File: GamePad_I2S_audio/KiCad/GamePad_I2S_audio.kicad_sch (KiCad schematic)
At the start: 75 parts, among them IC1 PCM5100, IC2 PAM8908, J1 Conn_02x17_Odd_Even

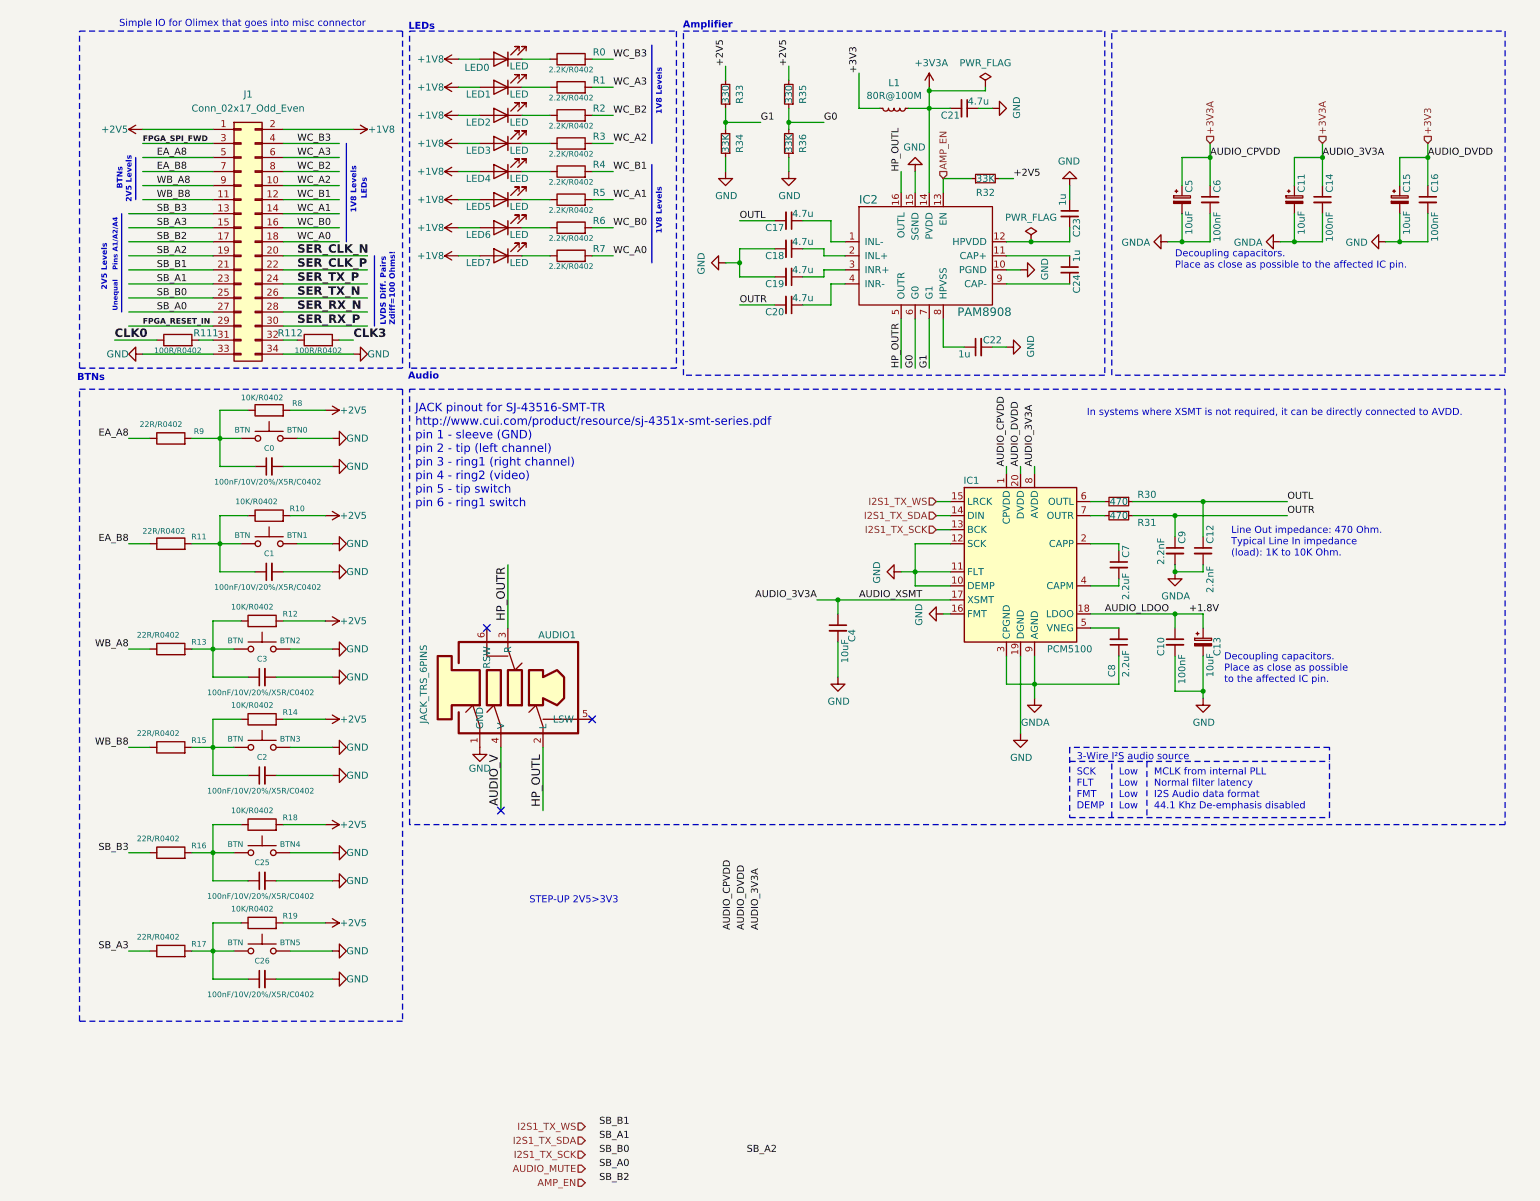
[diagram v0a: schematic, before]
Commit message: Adding StepUP
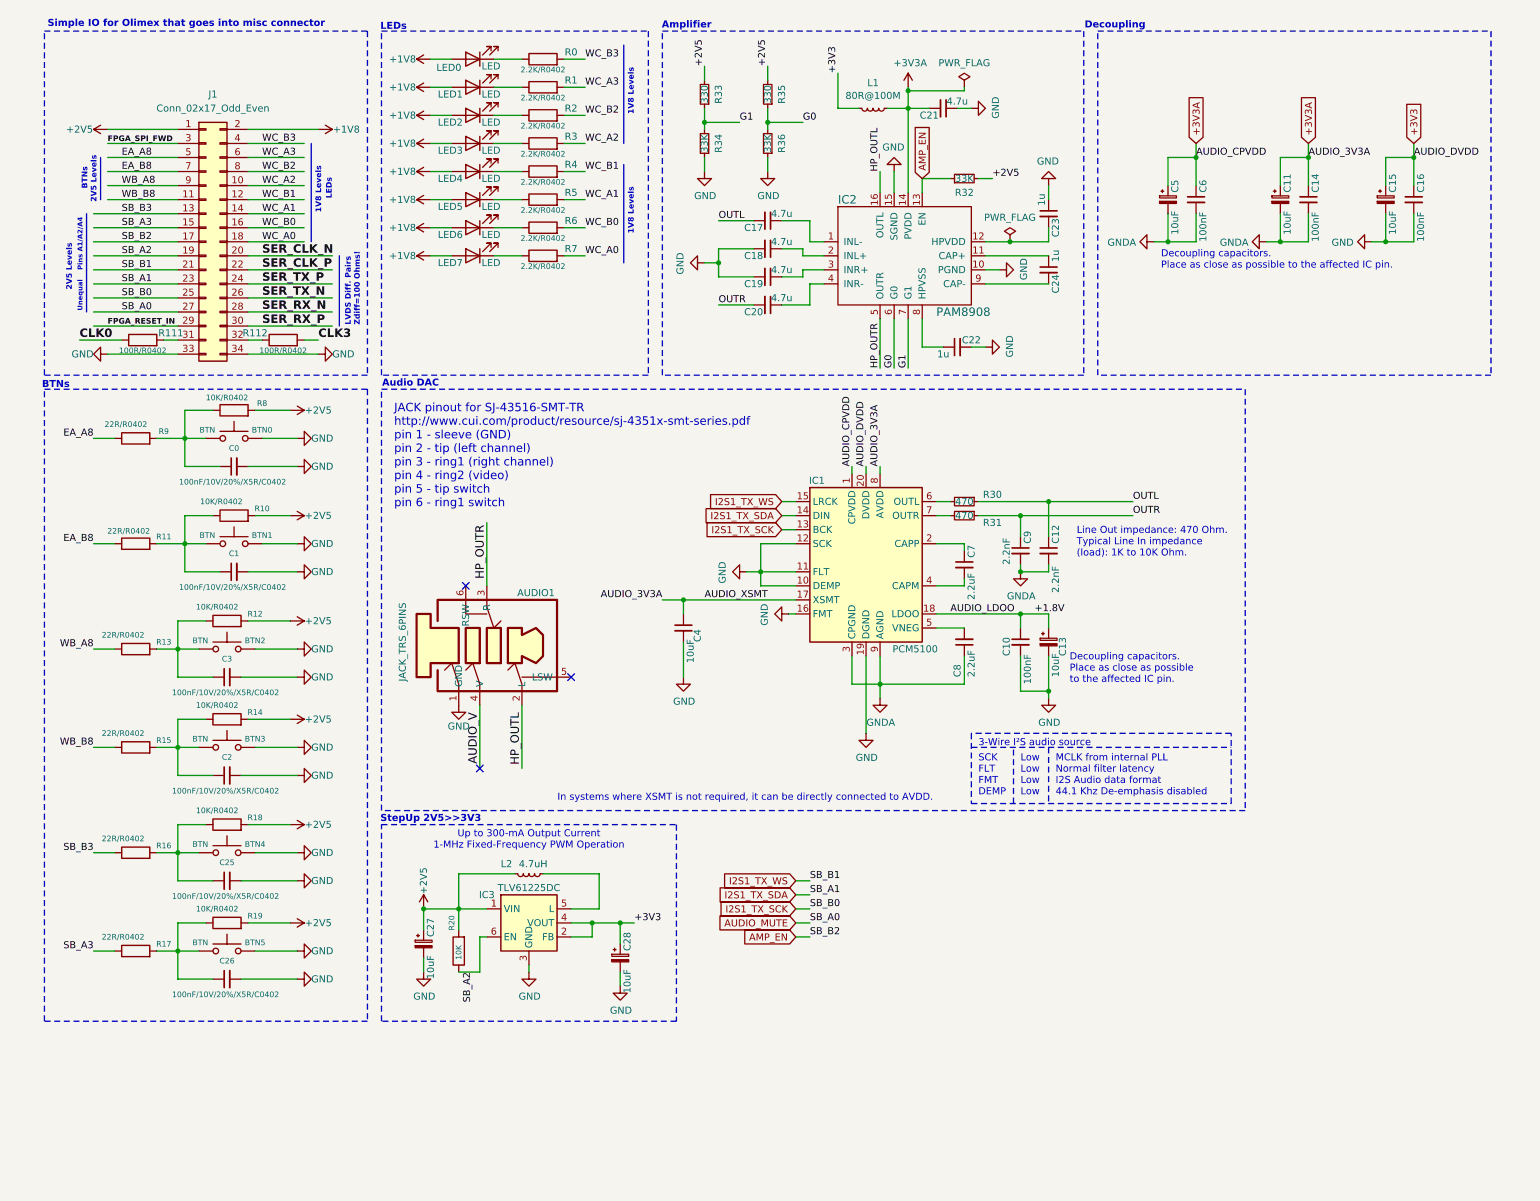
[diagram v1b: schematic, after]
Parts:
- added C27, C28: 10uF, Capacitor_SMD:C_1206_3216Metric, symbol Device:CP_Small
- added IC3: TLV61225DC, Package_TO_SOT_SMD:SOT-363_SC-70-6, symbol Regulator_Switching:TLV61225DC
- added L2: 4.7uH, Inductor_SMD:L_0603_1608Metric, symbol Device:L_Small
- added R20: 10K, Resistor_SMD:R_0603_1608Metric, symbol OLIMEX_RCL:R
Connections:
- net SB_A0 is gone; now on net AUDIO_MUTE: J1.27 (Pin_27)
- net SB_A1 is gone; now on net I2S1_TX_SDA: J1.23 (Pin_23)
- net SB_B0 is gone; now on net I2S1_TX_SCK: J1.25 (Pin_25)
- net SB_B1 is gone; now on net I2S1_TX_WS: J1.21 (Pin_21)
- net SB_B2 is gone; now on net AMP_EN: J1.17 (Pin_17)
- net +2V5: now also C27.1, IC3.1 (VIN), L2.2, R20.2
- net +3V3: now also C28.1, IC3.2 (FB), IC3.4 (VOUT)
- net GND: now also C27.2, C28.2, IC3.3 (GND)
- net SB_A2: now also IC3.6 (EN), R20.1
- new net: IC3.5 (L), L2.1
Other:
- note added: "Audio DAC"
- note added: "Decoupling"
- note added: "StepUp 2V5>>3V3"
- note added: "Up to 300-mA Output Current 1-MHz Fixed-Frequency PWM Operation"
- note removed: "Audio"
- note removed: "STEP-UP 2V5>3V3"
- company: (none) -> Intergalaktik d.o.o.
- title: (none) -> GamePad_I2S_Audio
- moved on the sheet: AUDIO1, BTN0, BTN1, BTN2, BTN3, BTN4, BTN5, C0, C1, C10, C11, C12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

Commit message: Adding initial schematics
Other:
- note added: "Audio"
- note removed: "Unequal Pins A1/A2/A4"
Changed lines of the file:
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@@
 	(polyline
 		(pts
-			(xy 22.86 49.53) (xy 22.86 67.31)
+			(xy 25.4 54.61) (xy 25.4 67.31)
 		)
 		(stroke
@@
 	(wire
 		(pts
-			(xy 24.13 54.61) (xy 39.37 54.61)
+			(xy 26.67 54.61) (xy 39.37 54.61)
 		)
 		(stroke
@@
 	(wire
 		(pts
-			(xy 24.13 62.23) (xy 39.37 62.23)
+			(xy 26.67 62.23) (xy 39.37 62.23)
 		)
 		(stroke
@@
 	(wire
 		(pts
-			(xy 24.13 52.07) (xy 39.37 52.07)
+			(xy 26.67 52.07) (xy 39.37 52.07)
 		)
 		(stroke
@@
 	(wire
 		(pts
-			(xy 24.13 64.77) (xy 39.37 64.77)
+			(xy 26.67 64.77) (xy 39.37 64.77)
 		)
 		(stroke
@@
 	(wire
 		(pts
-			(xy 24.13 59.69) (xy 39.37 59.69)
+			(xy 26.67 59.69) (xy 39.37 59.69)
 		)
 		(stroke
@@
 	(wire
 		(pts
-			(xy 24.13 67.31) (xy 39.37 67.31)
+			(xy 26.67 67.31) (xy 39.37 67.31)
 		)
 		(stroke
@@
 	(wire
 		(pts
-			(xy 24.13 49.53) (xy 39.37 49.53)
+			(xy 26.67 49.53) (xy 39.37 49.53)
 		)
 		(stroke
@@
 	(polyline
 		(pts
-			(xy 25.4 39.37) (xy 25.4 46.99)
+			(xy 25.4 39.37) (xy 25.4 52.07)
 		)
 		(stroke
@@
 	(wire
 		(pts
-			(xy 24.13 57.15) (xy 39.37 57.15)
+			(xy 26.67 57.15) (xy 39.37 57.15)
 		)
 		(stroke
@@
 	(text "2V5 Levels"
 		(exclude_from_sim no)
-		(at 20.32 63.5 90)
+		(at 24.892 65.024 90)
 		(effects
 			(font
@@
 		)
 	)
-	(text "Unequal	Pins A1/A2/A4"
+	(text "Audio"
 		(exclude_from_sim no)
-		(at 22.225 67.31 90)
+		(at 23.114 61.976 90)
 		(effects
 			(font
-				(size 0.889 0.889)
+				(size 1.016 1.016)
 				(bold yes)
 				(color 0 0 255 1)

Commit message: initial PCB setup
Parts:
- C0, C1, C10, C14, C16, C2, C25, C26, C3, C6: footprint Capacitor_SMD:C_0603_1608Metric -> Capacitor_SMD:C_0402_1005Metric
- C11, C13, C15, C27, C28, C4, C5: footprint Capacitor_SMD:C_1206_3216Metric -> Capacitor_SMD:C_0603_1608Metric
- R0, R1, R10, R11, R111, R112, R12, R13, R14, R15, R16, R17, R18, R19, R2, R20, R3, R4, R5, R6, R7, R8, R9: footprint Resistor_SMD:R_0603_1608Metric -> Resistor_SMD:R_0402_1005Metric
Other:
- note added: "Audio connections"
- note added: "Decoupling DAC"
- note removed: "Decoupling"
- moved on the sheet: J1, LED0, LED1, LED2, LED3, LED4, LED5, LED6, LED7, R0, R1, R111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

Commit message: Routing
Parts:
- added R21: 0R, Resistor_SMD:R_0402_1005Metric, symbol OLIMEX_RCL:R
- R20: Digikey (none) -> P1.10KHCT-ND; Koncar (none) -> FR002; LCSC (none) -> C269415; MNF1_URL (none) -> www.yageo.com; MPN (none) -> RC0603FR-071K1L; Mouse_r2 (none) -> 603-AC0603FR-071K1L; Mouser (none) -> 603-RC0603FR-071K1L; Newark (none) -> 65T8314
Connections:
- net GND: now also R21.1; no longer C18.2, C19.2
- net GNDA: now also C18.2, C19.2, R21.2

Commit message: Sqitching to only one GND
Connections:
- net GNDA is gone; now on net GND: C11.2, C12.2, C14.2, C18.2, C19.2, C5.2, C6.2, C8.1, C9.2, IC1.3 (CPGND), IC1.9 (AGND), R21.2
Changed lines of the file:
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@@
 			)
 		)
-		(property "Value" "GNDA"
+		(property "Value" "GND"
 			(at 191.897 118.6942 0)
 			(effects
@@
 			)
 		)
-		(property "Value" "GNDA"
+		(property "Value" "GND"
 			(at 132.6642 58.547 90)
 			(effects
@@
 			)
 		)
-		(property "Value" "GNDA"
+		(property "Value" "GND"
 			(at 232.9942 54.737 90)
 			(effects
@@
 			)
 		)
-		(property "Value" "GNDA"
+		(property "Value" "GND"
 			(at 212.6742 54.737 90)
 			(effects
@@
 			)
 		)
-		(property "Value" "GNDA"
+		(property "Value" "GND"
 			(at 166.497 141.5542 0)
 			(effects

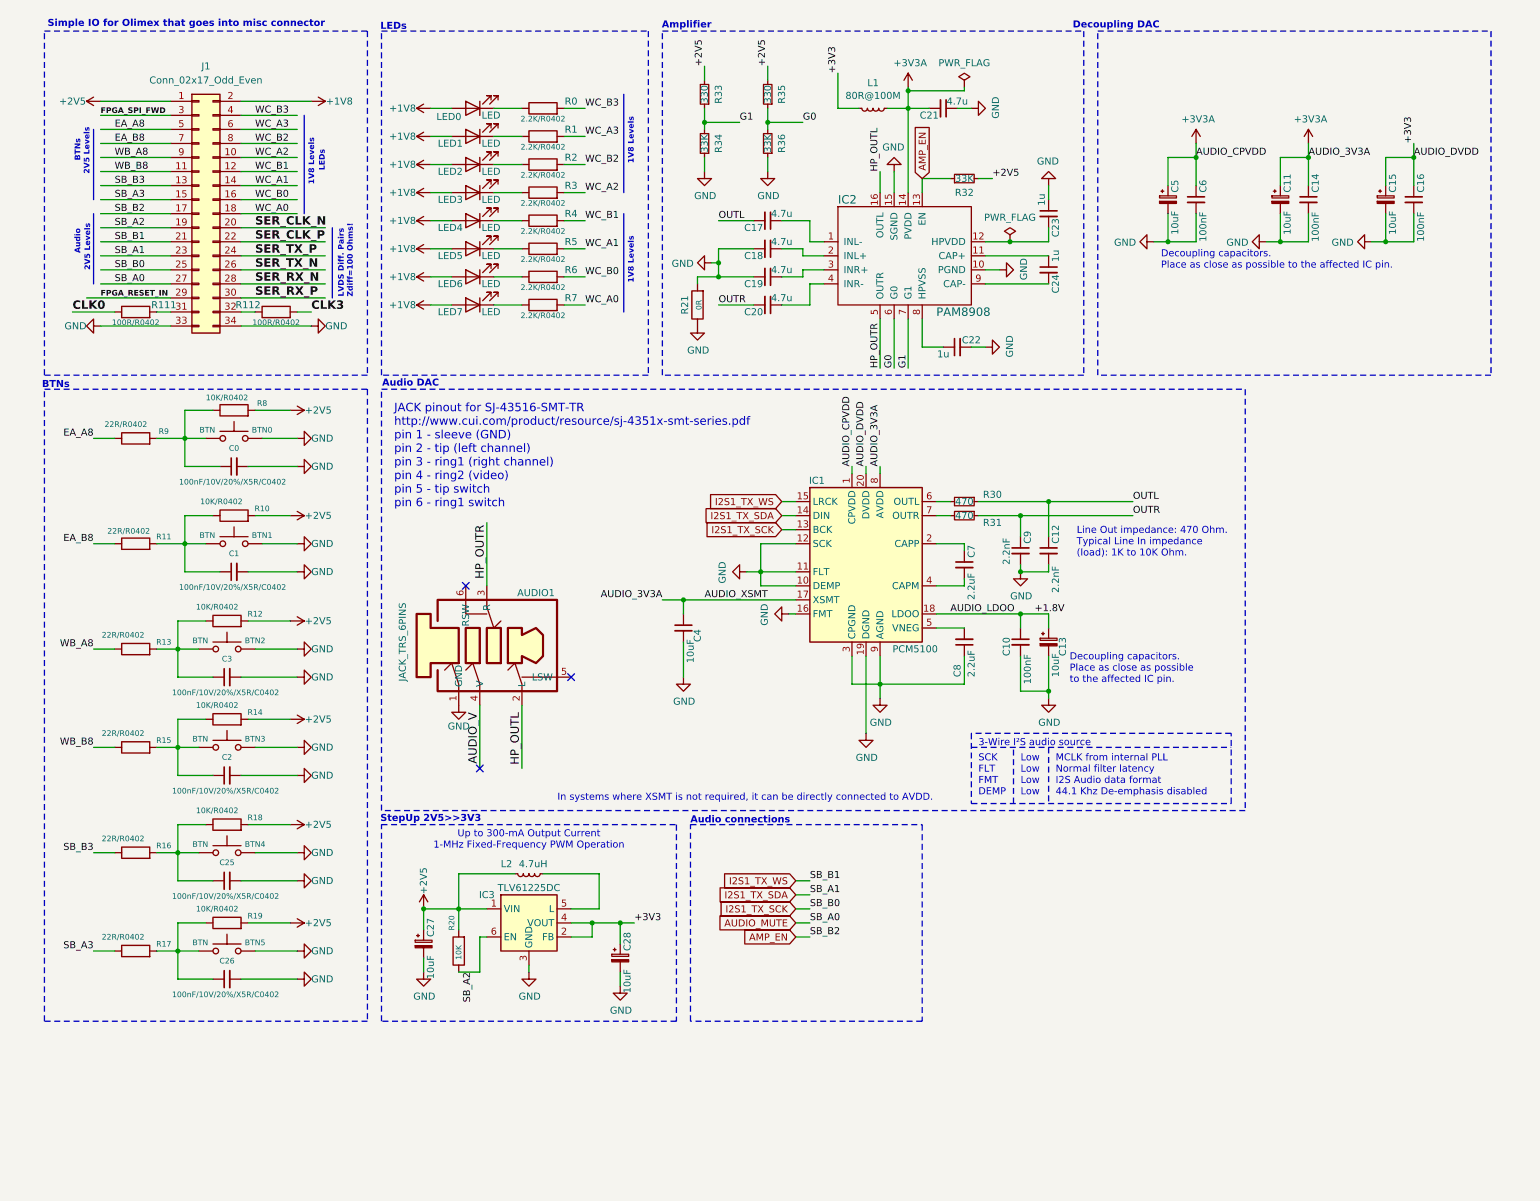
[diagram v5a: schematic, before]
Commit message: Moving schematics to v9 adding more details
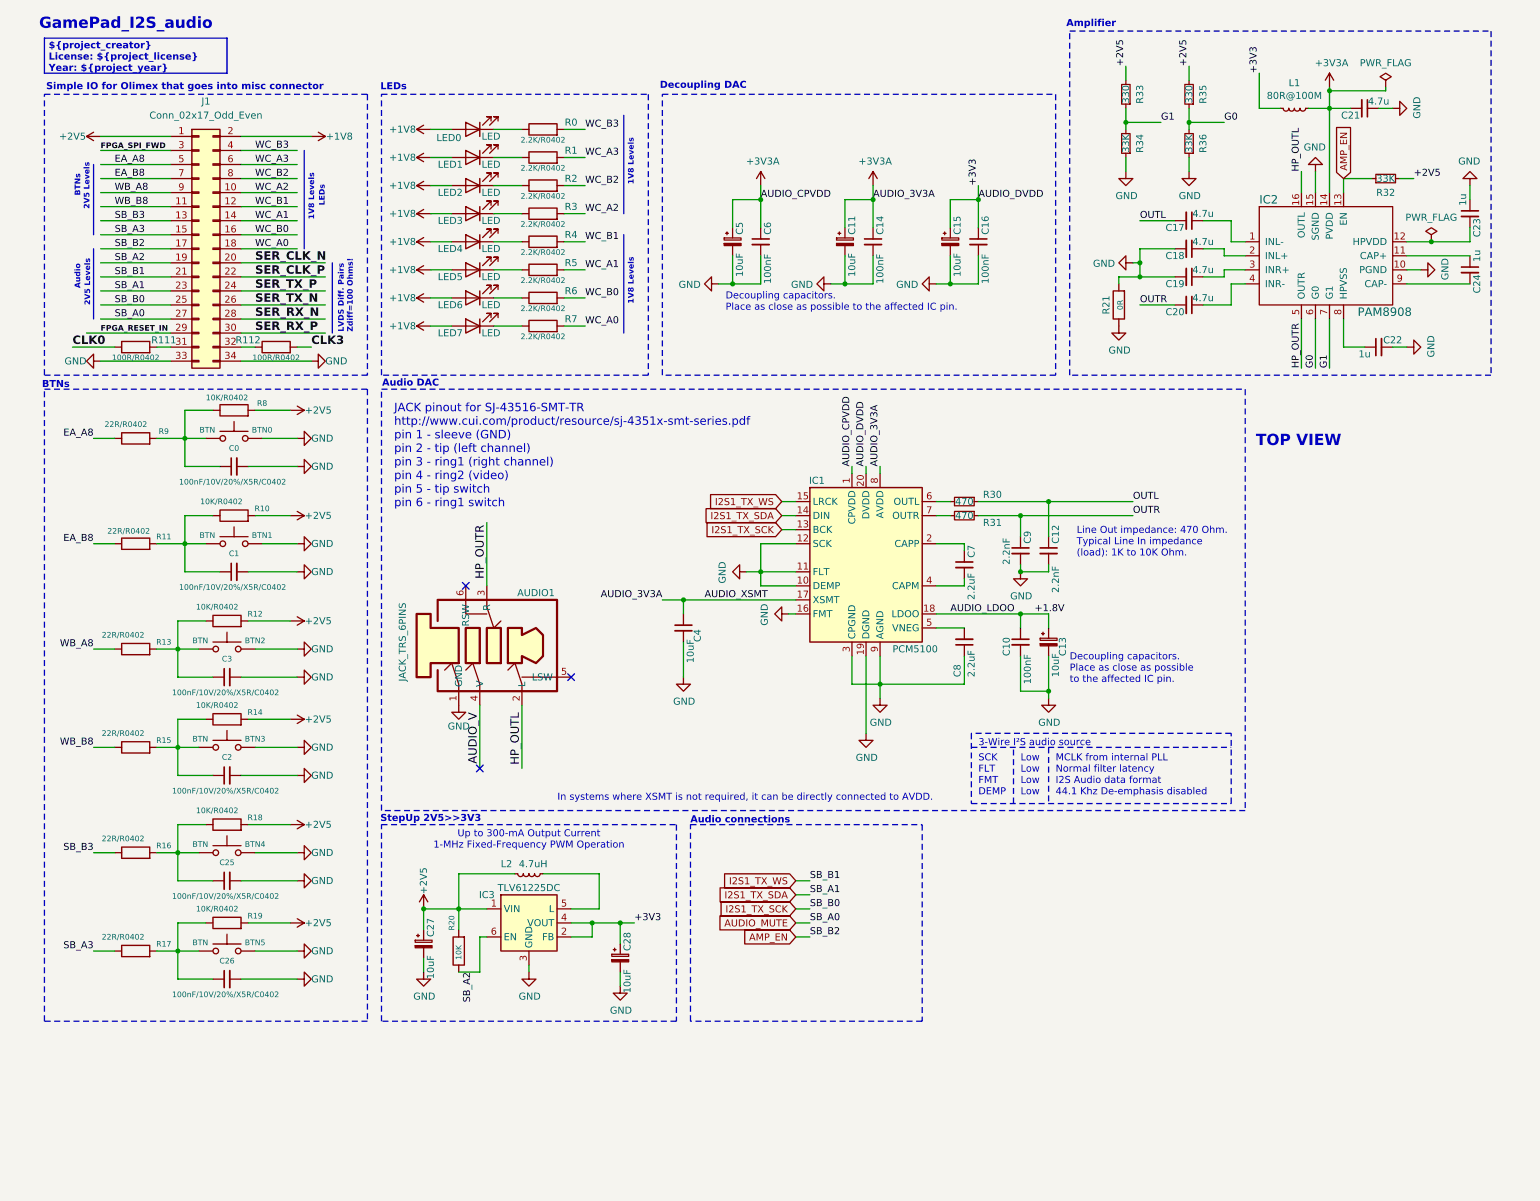
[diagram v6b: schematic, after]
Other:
- note added: "${project_creator} License: ${project_license} Year: ${project_year}"
- note added: "GamePad_I2S_audio"
- note added: "TOP VIEW"
- moved on the sheet: C11, C14, C15, C16, C17, C18, C19, C20, C21, C22, C23, C24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
